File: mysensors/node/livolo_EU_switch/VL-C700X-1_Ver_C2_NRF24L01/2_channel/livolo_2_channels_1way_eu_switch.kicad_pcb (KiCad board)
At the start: 2 copper layers, 43 x 43.4 mm, 50 parts, among them CON1 AVR-ISP-6, IC1 ATMEGA328P-AU, J1 DC-DC_EN, J2 3V_EN, P1 Sense Pad 1, P2 Sense Pad 2, P4 Power Board, U1 MIC5205-3.3, U2 MCP16301, U3 TTP223, U4 TTP223, U5 NRF24L01, U7 ATSHA204A

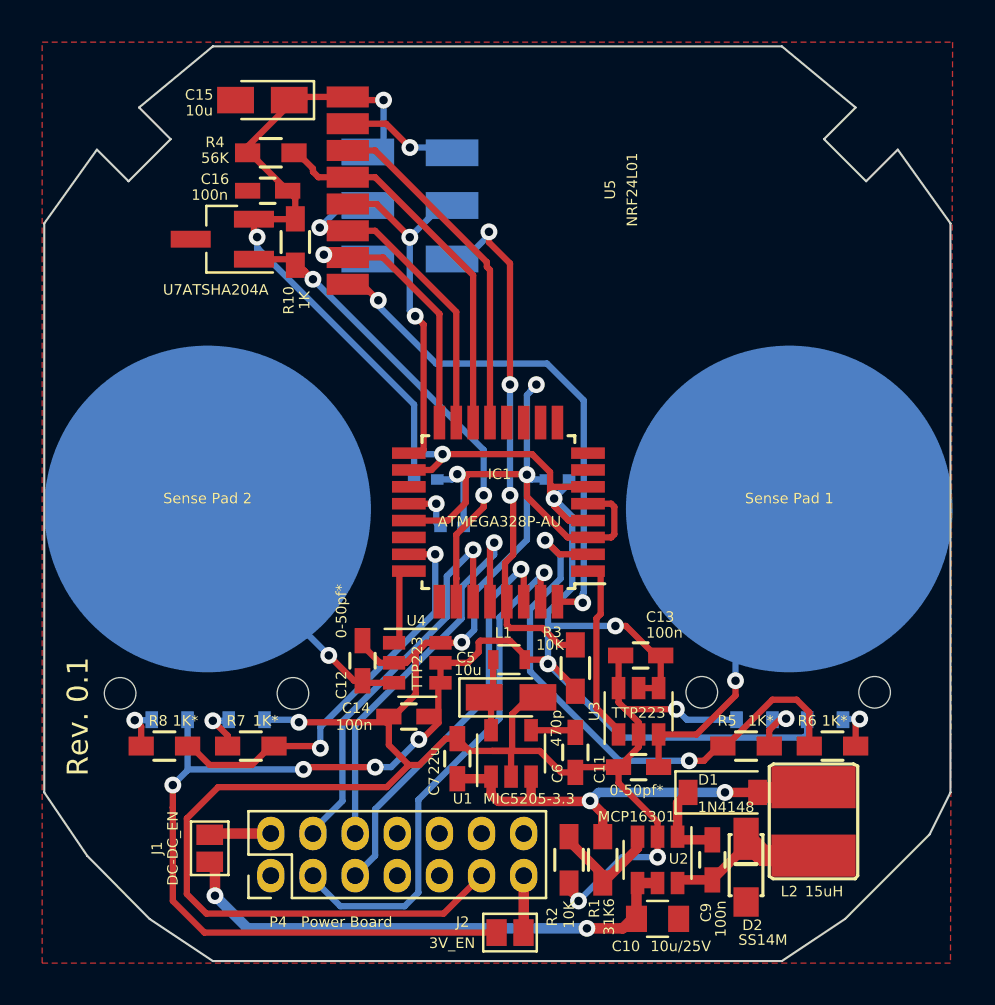
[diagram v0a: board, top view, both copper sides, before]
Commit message: refactorings - nrf24l01 livolo node
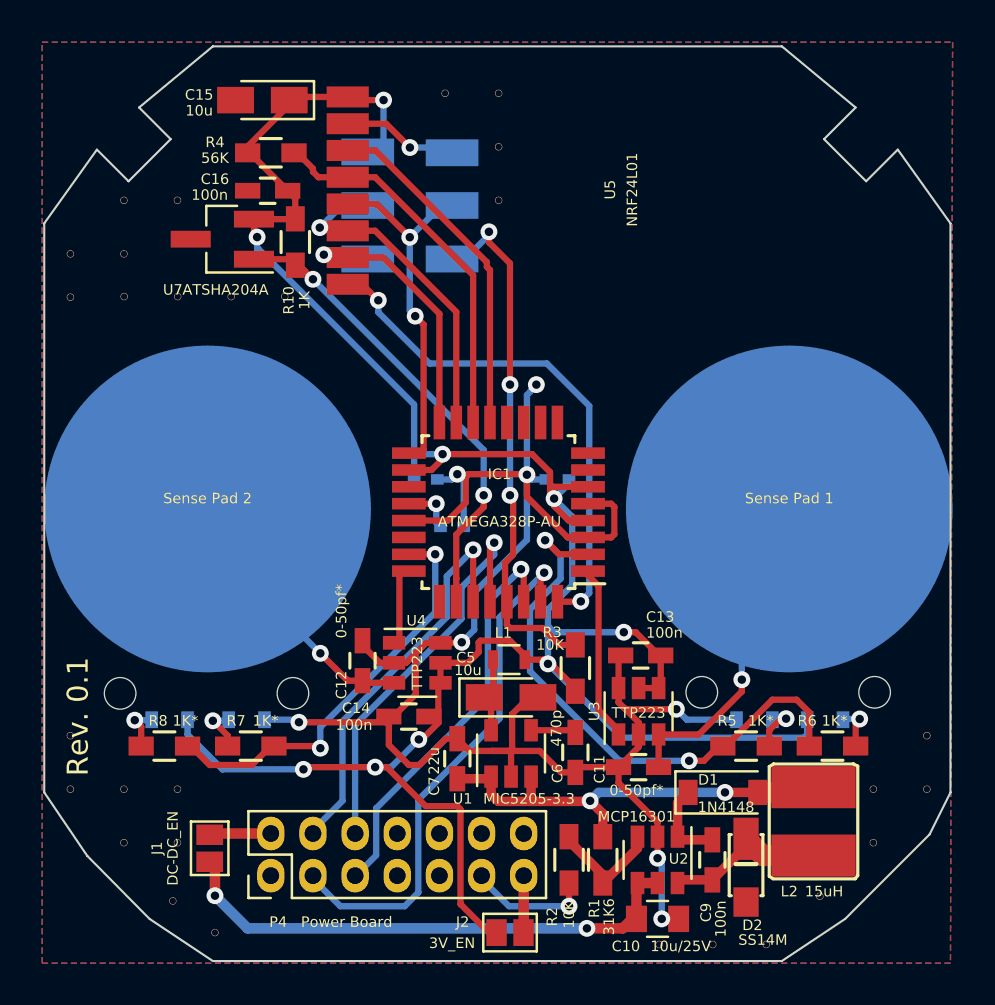
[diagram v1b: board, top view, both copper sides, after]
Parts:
- added V12_17: AUTO_VIA, VIA_MATRIX, F.Cu at (150.1, 112.8)
- added V13_17: AUTO_VIA, VIA_MATRIX, F.Cu at (152.6, 112.8)
- added V14_17: AUTO_VIA, VIA_MATRIX, F.Cu at (155.2, 112.8)
- added V15_16: AUTO_VIA, VIA_MATRIX, F.Cu at (157.7, 110.5)
- added V16_14: AUTO_VIA, VIA_MATRIX, F.Cu at (160.2, 105.4)
- added V16_15: AUTO_VIA, VIA_MATRIX, F.Cu at (160.2, 108.0)
- added V17_13: AUTO_VIA, VIA_MATRIX, F.Cu at (162.8, 102.9)
- added V17_14: AUTO_VIA, VIA_MATRIX, F.Cu at (162.8, 105.4)
- added V1_13: AUTO_VIA, VIA_MATRIX, F.Cu at (122.1, 102.9)
- added V1_14: AUTO_VIA, VIA_MATRIX, F.Cu at (122.1, 105.4)
- added V1_4: AUTO_VIA, VIA_MATRIX, F.Cu at (122.1, 80.0)
- added V1_5: AUTO_VIA, VIA_MATRIX, F.Cu at (122.1, 82.1)
- added V2_14: AUTO_VIA, VIA_MATRIX, F.Cu at (124.7, 105.4)
- added V2_15: AUTO_VIA, VIA_MATRIX, F.Cu at (124.7, 108.0)
- added V2_3: AUTO_VIA, VIA_MATRIX, F.Cu at (124.7, 77.5)
- added V2_4: AUTO_VIA, VIA_MATRIX, F.Cu at (124.7, 80.0)
- added V2_5: AUTO_VIA, VIA_MATRIX, F.Cu at (124.7, 82.1)
- added V3_14: AUTO_VIA, VIA_MATRIX, F.Cu at (127.2, 105.4)
- added V3_15: AUTO_VIA, VIA_MATRIX, F.Cu at (127.2, 108.0)
- added V3_16: AUTO_VIA, VIA_MATRIX, F.Cu at (127.0, 110.8)
- added V3_3: AUTO_VIA, VIA_MATRIX, F.Cu at (127.2, 77.5)
- added V3_5: AUTO_VIA, VIA_MATRIX, F.Cu at (127.2, 82.1)
- added V4_17: AUTO_VIA, VIA_MATRIX, F.Cu at (129.0, 112.2)
- added V4_5: AUTO_VIA, VIA_MATRIX, F.Cu at (129.8, 82.1)
- added V5_5: AUTO_VIA, VIA_MATRIX, F.Cu at (132.3, 82.1)
- added V8_1: AUTO_VIA, VIA_MATRIX, F.Cu at (139.9, 72.4)
- added V9_1: AUTO_VIA, VIA_MATRIX, F.Cu at (142.5, 72.4)
- added V9_2: AUTO_VIA, VIA_MATRIX, F.Cu at (142.5, 75.0)
- added V9_3: AUTO_VIA, VIA_MATRIX, F.Cu at (142.5, 77.5)
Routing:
- net GND: track 128.1 -> 102.3 mm, vias 9 -> 10
- net +3V3: track 128.9 -> 117.2 mm, vias 10 -> 9
- net /Relay2_Set: track 19.4 -> 20.0 mm
- added copper zone on B.Cu, net GND
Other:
- net class Default: clearance 0.25 -> 0.2
- rule trace_clearance: 0.25 -> 0.2
